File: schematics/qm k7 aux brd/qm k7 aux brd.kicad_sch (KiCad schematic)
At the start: 27 parts, among them J1 LEFT, J2 Micro_SD_Card, J3 Conn_01x03, J4 Conn_01x03, U1 AP1117-33, U2 CS4344-CZZ

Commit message: Rv32: QM K7 aux schematic and STM32 breakout schematic. Both ordered.
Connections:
- net I2S_LRCK: now also J1.50 (Pin_50); no longer J1.48 (Pin_48)
- net I2S_MCLK: now also J1.52 (Pin_52); no longer J1.46 (Pin_46)
- net I2S_SCLK: now also J1.48 (Pin_48); no longer J1.50 (Pin_50)
- net I2S_SDIN: now also J1.46 (Pin_46); no longer J1.52 (Pin_52)
- net SD_CLK: now also J1.53 (Pin_53); no longer J1.57 (Pin_57)
- net SD_CMD: now also J1.55 (Pin_55); no longer J1.59 (Pin_59)
- net SD_DAT0: now also J1.51 (Pin_51); no longer J1.55 (Pin_55)
- net SD_DAT1: now also J1.49 (Pin_49); no longer J1.53 (Pin_53)
- net SD_DAT2: now also J1.59 (Pin_59); no longer J1.51 (Pin_51)
- net SD_DAT3: now also J1.57 (Pin_57); no longer J1.49 (Pin_49)
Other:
- moved on the sheet: C7, C8, C9, U2

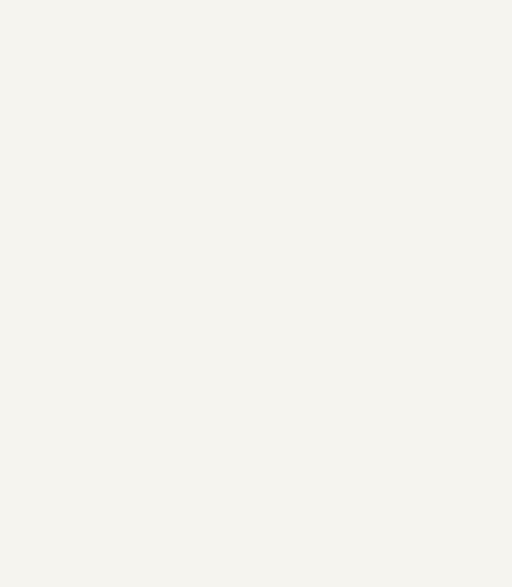
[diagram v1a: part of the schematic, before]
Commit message: Rv32: Audio over I2S working.
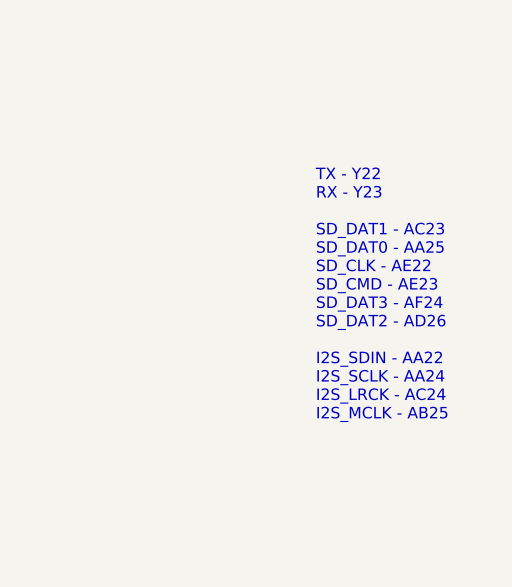
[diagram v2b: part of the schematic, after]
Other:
- note added: "TX - Y22 RX - Y23 SD_DAT1 - AC23 SD_DAT0 - AA25 SD_CLK - AE22 SD_CMD - AE23 SD_DAT3 - AF24 SD_DAT2 - AD26 I2S_SDIN - AA22 I2S_SCLK - AA24 I2S_LRCK - AC24 I2S_MCLK - AB25"
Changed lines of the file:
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@@
     (stroke (width 0) (type default) (color 0 0 0 0))
+  )
+  (text "TX - Y22\nRX - Y23\n\nSD_DAT1 - AC23\nSD_DAT0 - AA25\nSD_CLK - AE22\nSD_CMD - AE23\nSD_DAT3 - AF24\nSD_DAT2 - AD26\n\nI2S_SDIN - AA22\nI2S_SCLK - AA24\nI2S_LRCK - AC24\nI2S_MCLK - AB25"
+    (at 303.53 114.3 0)
+    (effects (font (size 1.27 1.27)) (justify left bottom))
   )
   (text "5V at 63 & 64 from board" (at 222.25 125.73 0)
